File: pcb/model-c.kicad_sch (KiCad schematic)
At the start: 143 parts, among them IC1 HT16K33, IC2 HT16K33, J1 Batt, J2 Conn_01x02_Socket, J3 Conn_01x02_Socket, SW1 SW_SPST, SW10 SW_SPST, SW11 SW_SPST, SW12 SW_SPST, SW13 SW_SPST, SW14 SW_SPST, SW15 SW_SPST, SW16 SW_SPST, SW17 SW_SPST, SW18 SW_SPST, SW19 SW_SPST, SW2 SW_SPST, SW21 SW_SPDT, SW3 SW_SPST, SW4 SW_SPST, SW5 SW_SPST, SW6 SW_SPST, SW7 SW_SPST, SW8 SW_SPST, SW9 SW_SPST, U1 W25Q16JVUXIQ, U11 TPS63070RNMR, U2 14seg, U2 TLV75533PDBVR, U3 RP2040, U4 MCP73831-2-OT, U5 TPS61090, U6 14seg, U8 TPS2115APW, U9 TPS2115APW, Y1 12MHz

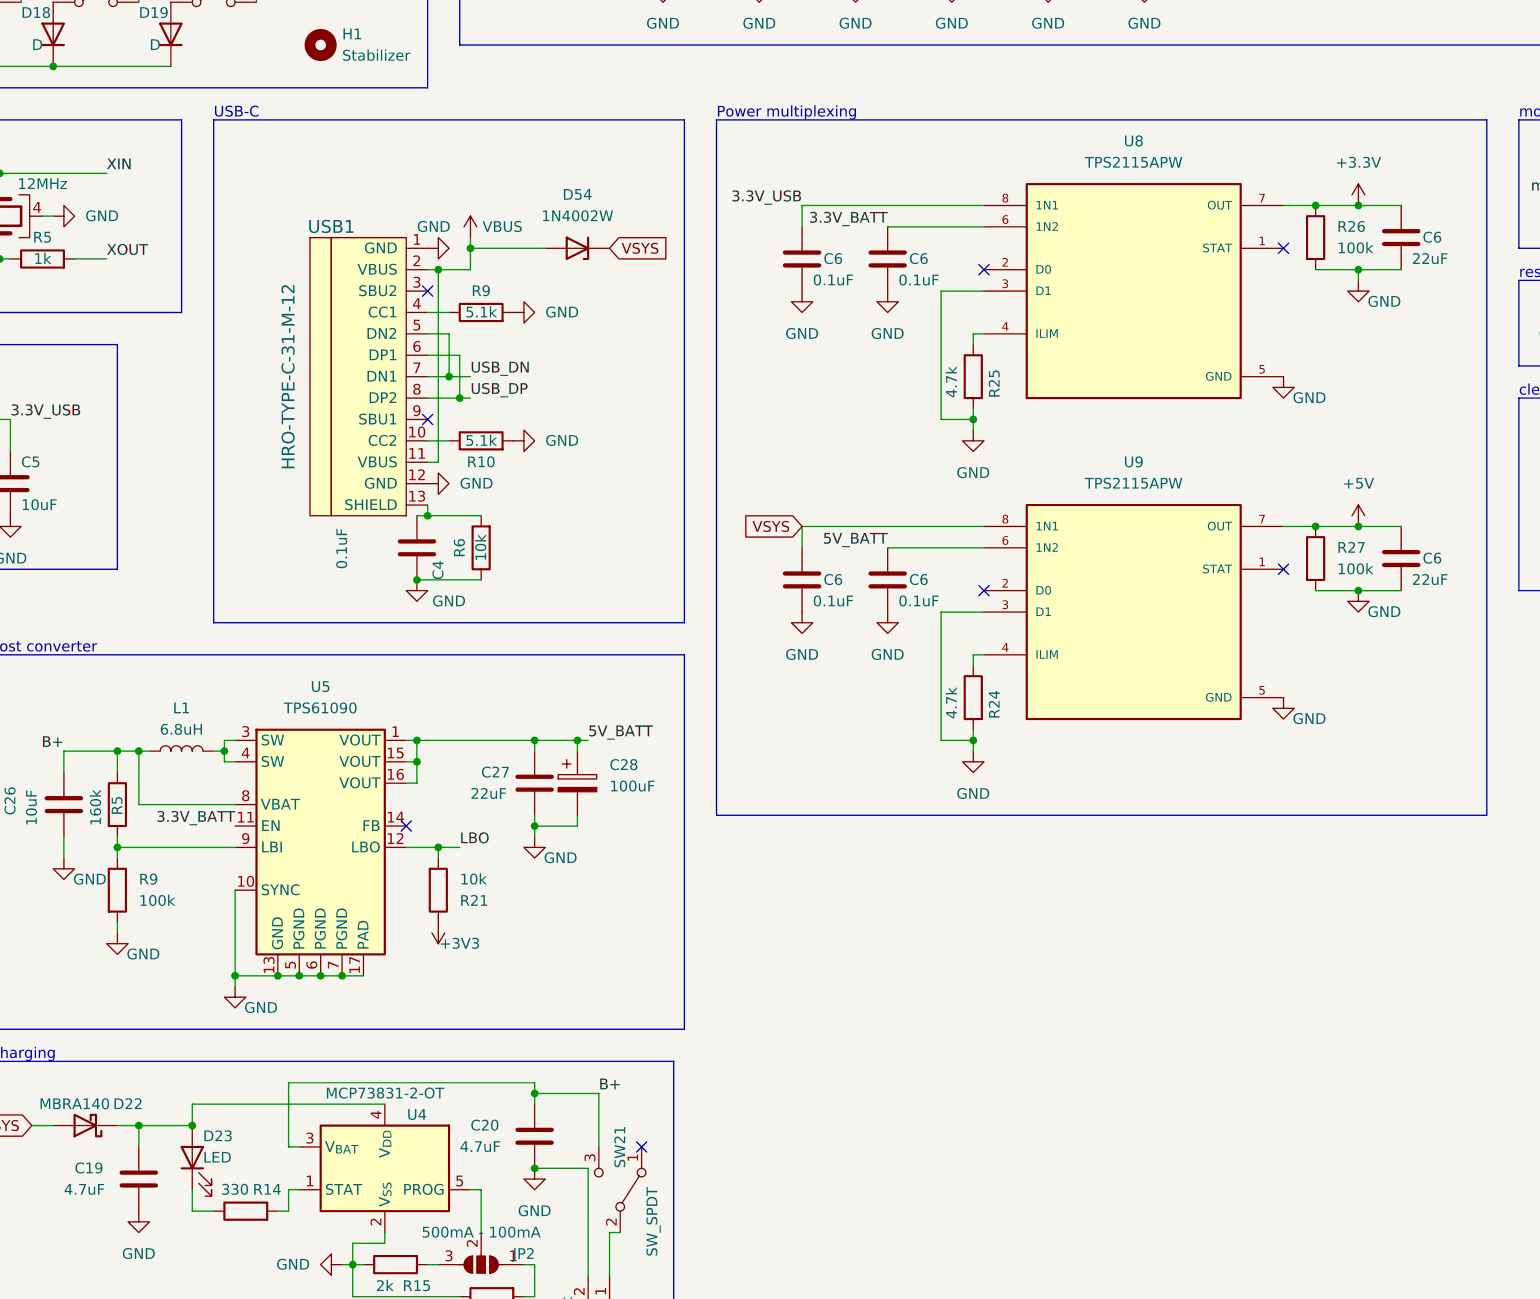
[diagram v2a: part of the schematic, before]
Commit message: fixing battery charger from backfeeding, battery 3.3V regulation, 5V boost converter, and power multiplexing
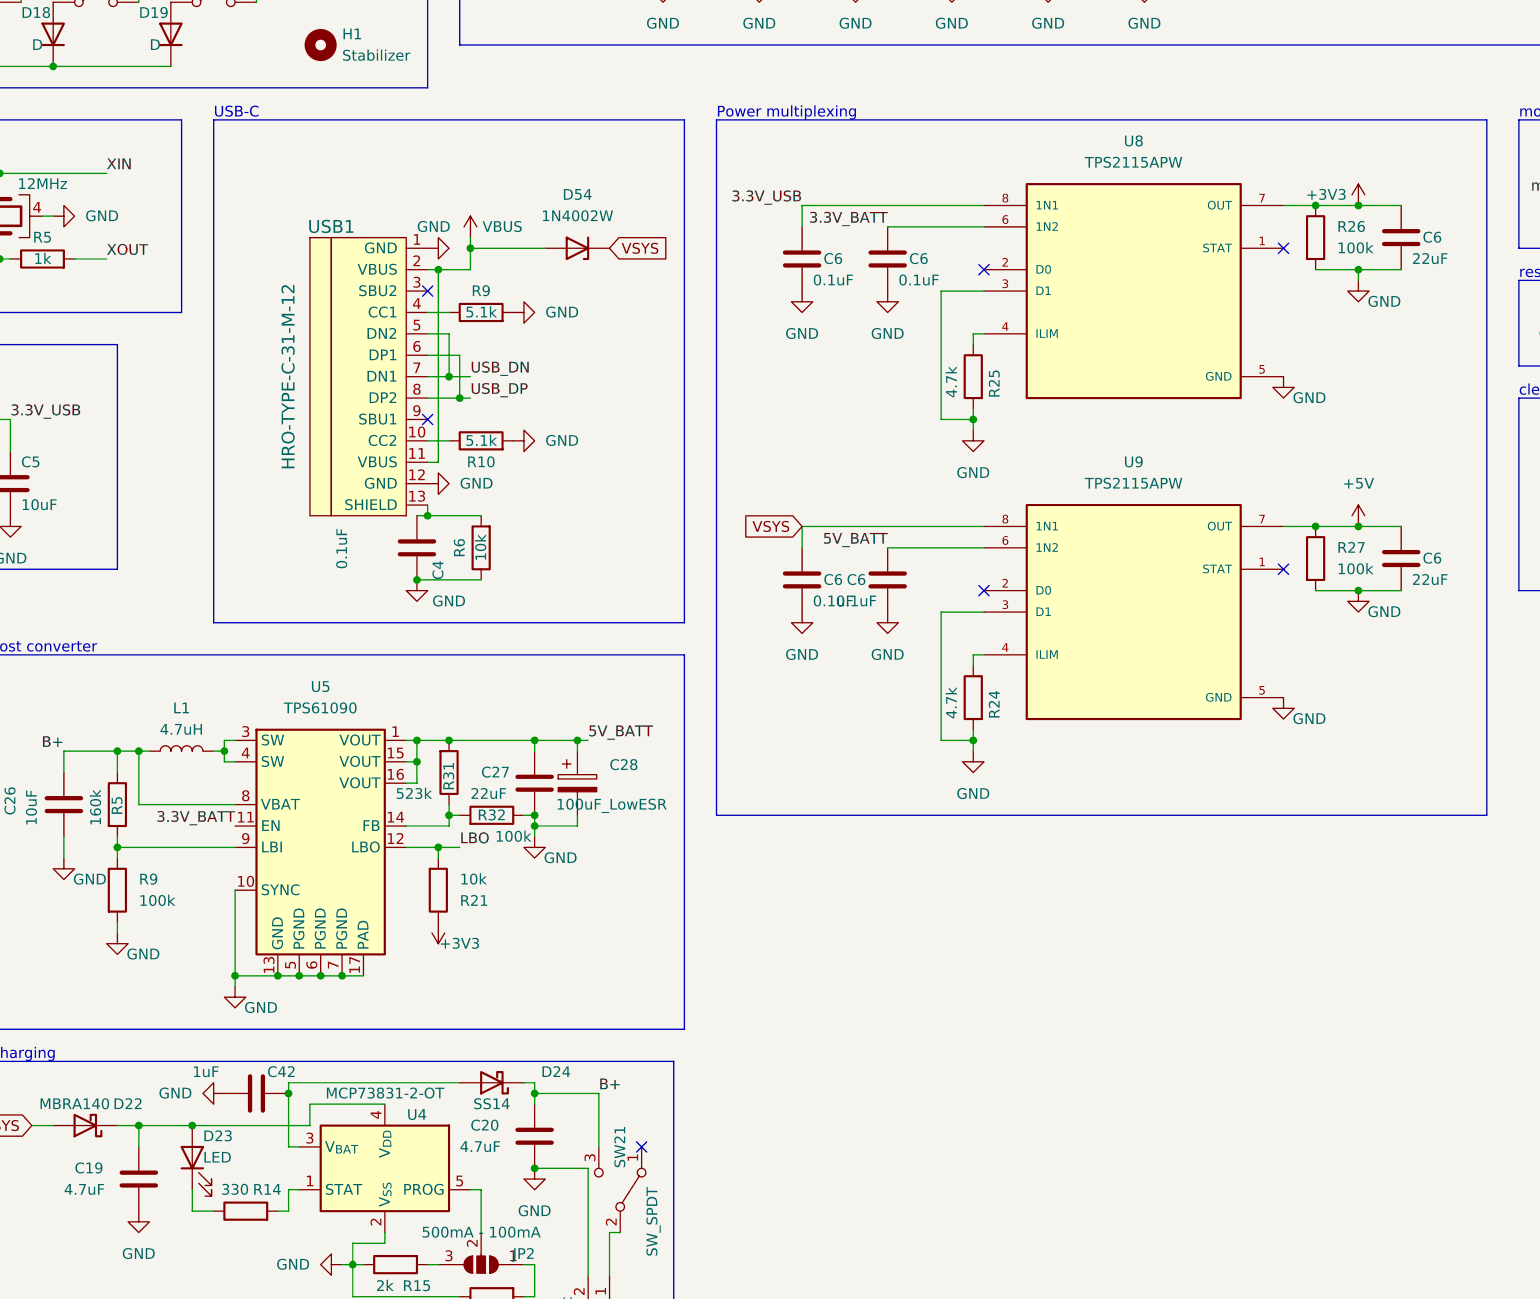
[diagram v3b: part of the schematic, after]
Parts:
- added C42: 1uF, Capacitor_SMD:C_0402_1005Metric, symbol Device:C
- added D24: SS14, Diode_SMD:D_SMA, symbol Device:D_Schottky
- added R31: 523k, Resistor_SMD:R_0402_1005Metric, symbol Device:R
- added R32: 100k, Resistor_SMD:R_0402_1005Metric, symbol Device:R
- C26, C27, C34, C37, C38, C39, C40, C41: footprint (none) -> Capacitor_SMD:C_0402_1005Metric
- C28: value 100uF -> 100uF_LowESR; footprint (none) -> Capacitor_SMD:C_0402_1005Metric
- L1: value 6.8uH -> 4.7uH; footprint (none) -> Inductor_SMD:L_Sunlord_MWSA0503S
- L2: footprint (none) -> Inductor_SMD:L_Coilcraft_XxL4020
- R21, R23, R26, R27, R28, R29, R30, R5, R9: footprint (none) -> Resistor_SMD:R_0402_1005Metric
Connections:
- net +3.3V is gone; now on net +3V3: C6.1, R26.1, U8.7 (OUT)
- net 5V_BATT: now also R31.2
- net B+: now also D24.1 (K); no longer U4.3 (V_{BAT})
- net GND: now also C42.2, R32.1
- net at U5.14 (FB): now also R31.1, R32.2
- new net: C42.1, D24.2 (A), U4.3 (V_{BAT})
- no-connect marks 40 -> 39

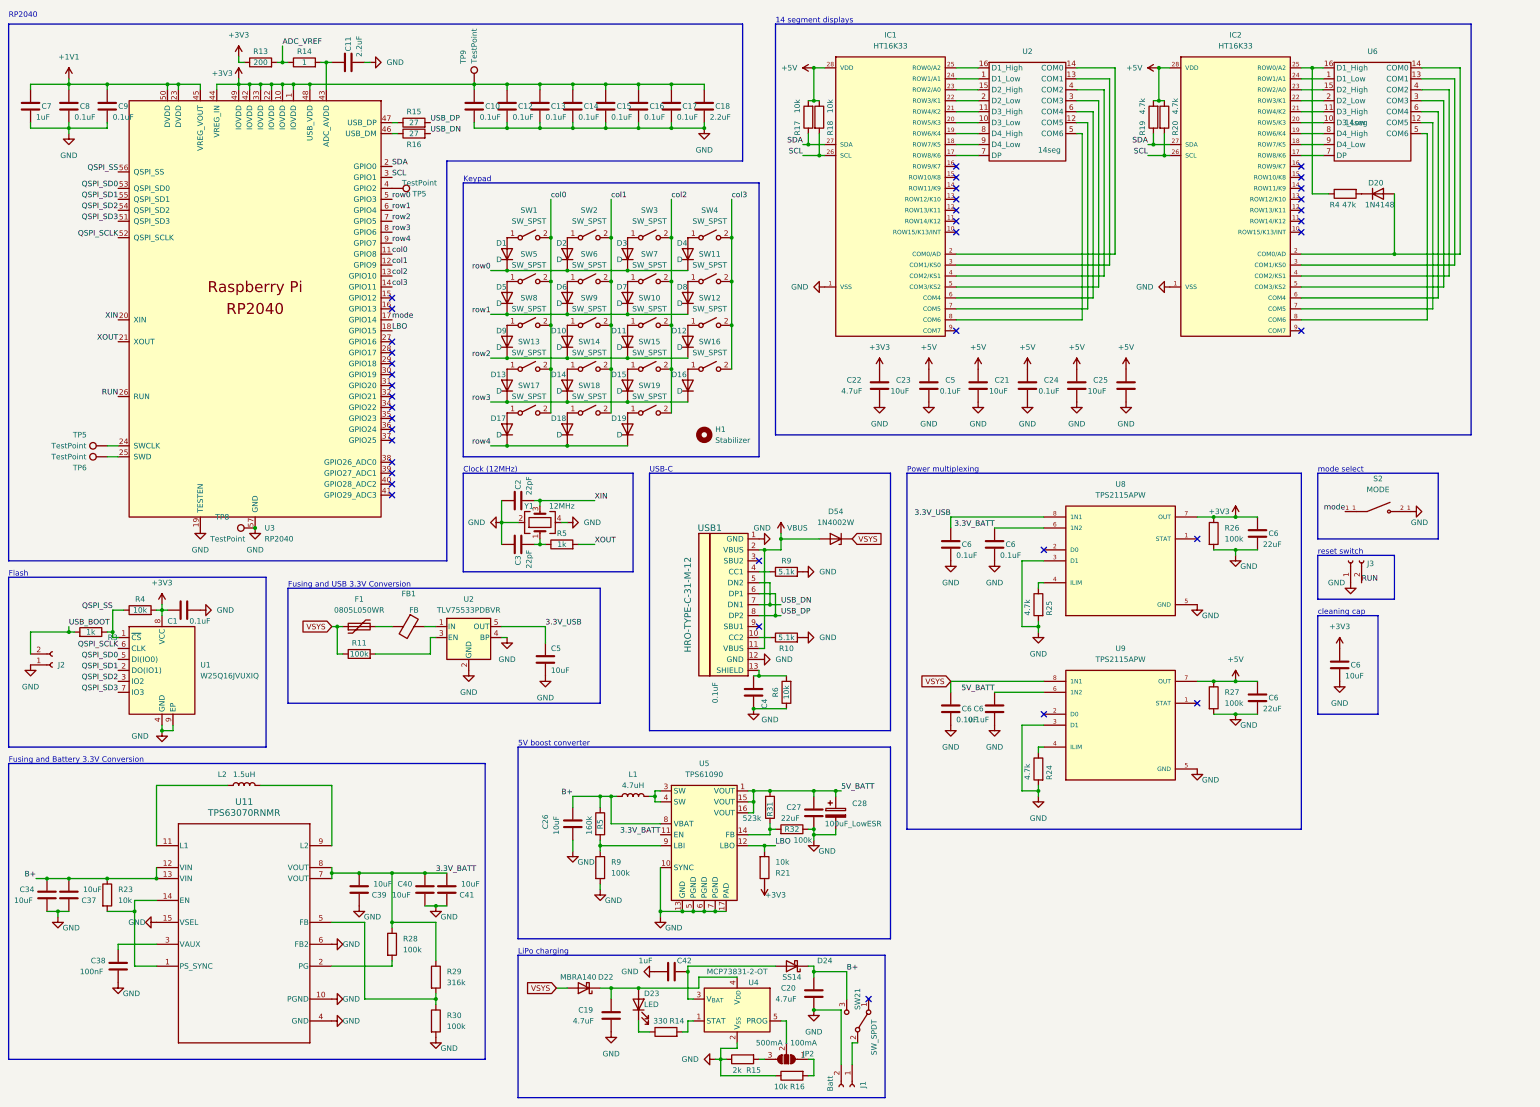
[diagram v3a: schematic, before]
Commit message: housing complete and PCB validated. need further validation and revisions of housing, as well as BOM to continue. updated PCB to rev. 2.1
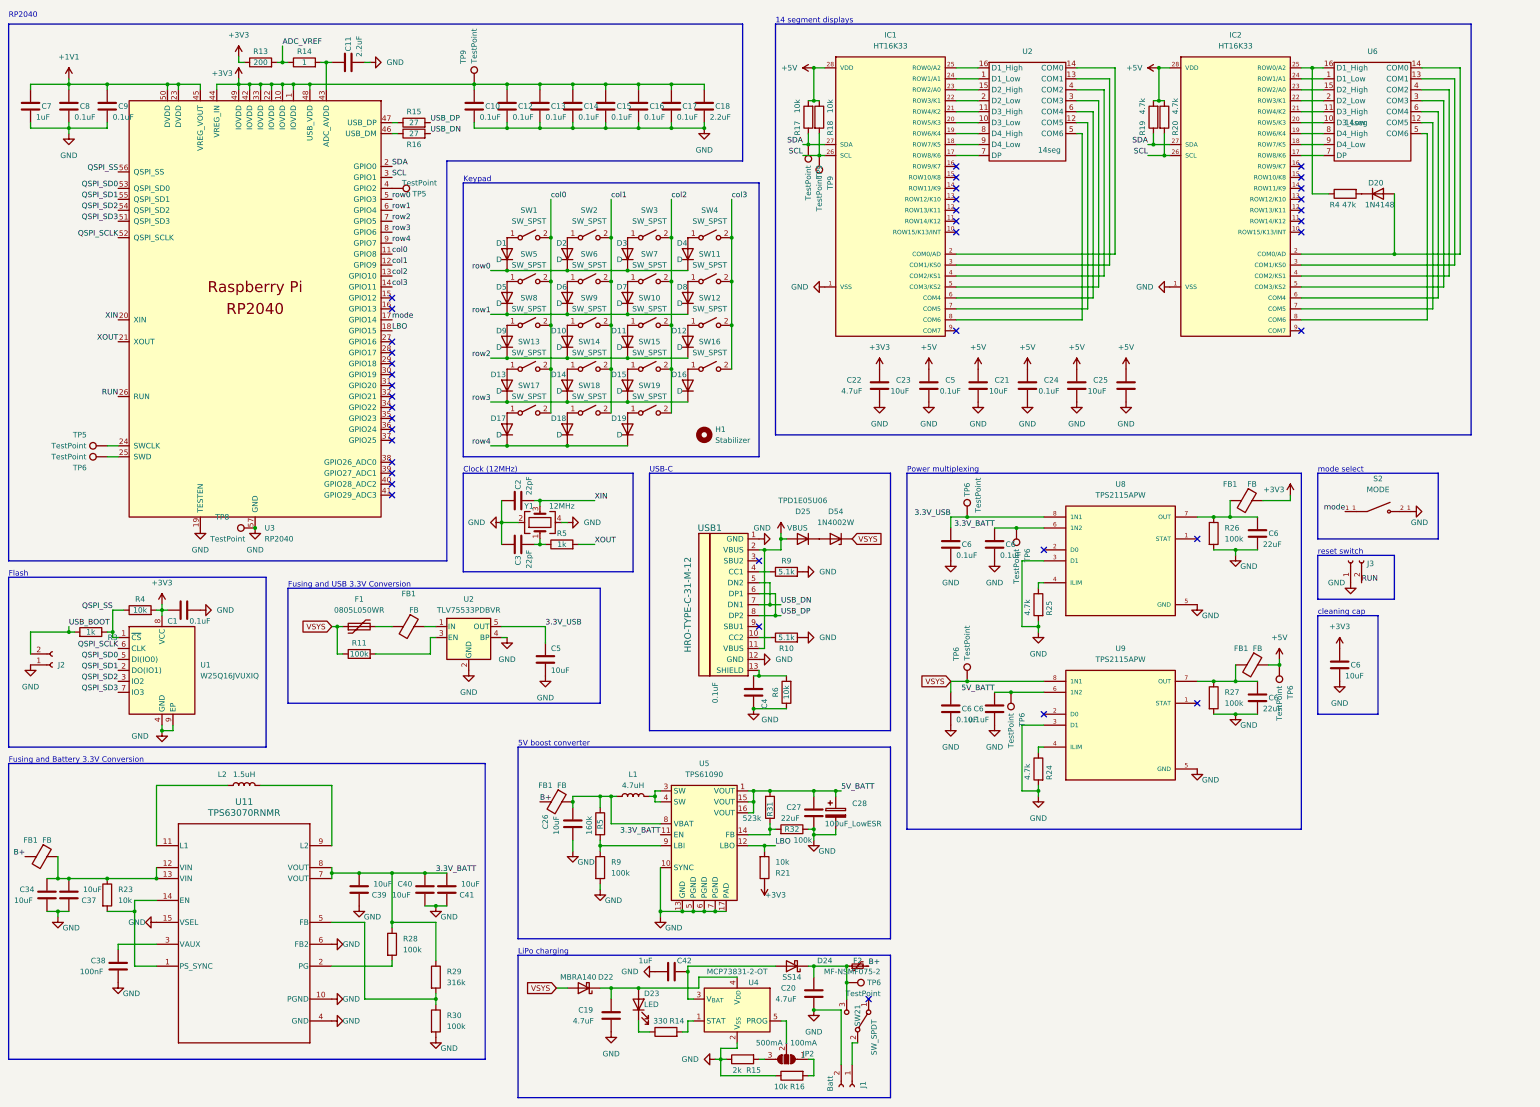
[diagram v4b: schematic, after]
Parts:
- added D25: TPD1E05U06, footprints:RTVS_DFN1006-2_SOD882_NEX, symbol Device:D
- added F2: MF-NSMF075-2, Fuse:Fuse_1206_3216Metric, symbol Device:Polyfuse_Small
- added FB1 (x4): FB, Resistor_SMD:R_0402_1005Metric, symbol Device:FerriteBead
- added TP6 (x6), TP9 (x2): TestPoint, libraries:CustomTestPoint, symbol Connector:TestPoint
- U11: footprint RNM0015A -> footprints2:RNM0015A
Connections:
- net +3V3: now also FB1.1; no longer C6.1, R26.1, U8.7 (OUT)
- net +5V: now also FB1.1, TP6.1; no longer C6.1, R27.1, U9.7 (OUT)
- net 3.3V_BATT: now also TP6.1
- net 3.3V_USB: now also TP6.1
- net 5V_BATT: now also TP6.1
- net B+: now also F2.2, FB1.2, FB1.2; no longer C20.1, C26.1, C34.1, C37.2, D24.1 (K), L1.1, R23.1, R5.1, SW21.3 (C), U11.12 (VIN), U11.13 (VIN), U5.8 (VBAT)
- net SCL: now also TP9.1
- net SDA: now also TP9.1
- net VBUS: now also D25.2 (A); no longer D54.2 (A)
- net VSYS: now also TP6.1
- new net: C26.1, FB1.1, L1.1, R5.1, U5.8 (VBAT)
- new net: C34.1, C37.2, FB1.1, R23.1, U11.12 (VIN), U11.13 (VIN)
- new net: C20.1, D24.1 (K), F2.1, SW21.3 (C), TP6.1
- new net: C6.1, FB1.2, R26.1, U8.7 (OUT)
- new net: D25.1 (K), D54.2 (A)
- new net: C6.1, FB1.2, R27.1, U9.7 (OUT)

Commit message: updates to pcb and addition of display code. I may rewrite the calculator code
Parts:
- removed D20: 1N4148, Diode_SMD:D_SOD-123, symbol Device:D
- removed R17, R18: 10k, Resistor_SMD:R_0402_1005Metric, symbol Device:R
- removed R19, R20: 4.7k, Resistor_SMD:R_0402_1005Metric, symbol Device:R
- removed U2, U6: 14seg, hk:14 seg, symbol HT16K33:COM-21216
- added DS1, DS2: TDCG1060M, libraries2:DISPLAY_TDCG1060M, symbol TDCG1060M:TDCG1060M
- added R33, R34: 4.7k, Resistor_SMD:R_0402_1005Metric, symbol Device:R
- added TP9 (x2): TestPoint, libraries:CustomTestPoint, symbol Connector:TestPoint
- added U10: TXS0102DCU, Package_SO:VSSOP-8_2.3x2mm_P0.5mm, symbol Logic_LevelTranslator:TXS0102DCU
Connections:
- net +3V3: now also U10.3 (VCCA), U10.6 (OE)
- net +5V: now also R4.2, R33.1, R34.2, U10.7 (VCCB)
- net GND: now also U10.2 (GND)
- net at IC1.15 (ROW10/K8): now also DS2.7
- net at IC1.16 (ROW9/K7): now also DS2.15
- net at IC1.17 (ROW8/K6): now also DS2.11
- net at IC1.18 (ROW7/K5): now also DS2.5
- net at IC1.19 (ROW6/K4): now also DS2.3
- net at IC1.2 (COM0/AD): now also DS2.1
- net at IC1.20 (ROW5/K3): now also DS2.13
- net at IC1.21 (ROW4/K2): now also DS2.16
- net at IC1.22 (ROW3/K1): now also DS2.14
- net at IC1.3 (COM1/KS0): now also DS2.2
- net at IC1.4 (COM2/KS1): now also DS2.6
- net at IC1.5 (COM3/KS2): now also DS2.8
- net at IC2.15 (ROW10/K8): now also DS1.7
- net at IC2.16 (ROW9/K7): now also DS1.15
- net at IC2.17 (ROW8/K6): now also DS1.11
- net at IC2.18 (ROW7/K5): now also DS1.5
- net at IC2.19 (ROW6/K4): now also DS1.3
- net at IC2.2 (COM0/AD): now also DS1.1
- net at IC2.20 (ROW5/K3): now also DS1.13
- net at IC2.21 (ROW4/K2): now also DS1.16
- net at IC2.22 (ROW3/K1): now also DS1.14
- net at IC2.23 (ROW2/A0): now also R4.1
- net at IC2.25 (ROW0/A2): no longer R4.1
- net at IC2.3 (COM1/KS0): now also DS1.2
- net at IC2.4 (COM2/KS1): now also DS1.6
- net at IC2.5 (COM3/KS2): now also DS1.8
- net SCL renamed SCL_5V
- net SCL_5V: now also R33.2, U10.1 (B2); no longer U3.3 (GPIO1)
- net SDA renamed SDA_5V
- net SDA_5V: now also R34.1, U10.8 (B1); no longer U3.2 (GPIO0)
- new net SCL_3.3V: TP9.1, U10.4 (A2), U3.3 (GPIO1)
- new net SDA_3.3V: TP9.1, U10.5 (A1), U3.2 (GPIO0)
- no-connect marks 39 -> 54
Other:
- note added: "I2C Level Shifter"
- moved on the sheet: IC1, IC2, R4, TP9
